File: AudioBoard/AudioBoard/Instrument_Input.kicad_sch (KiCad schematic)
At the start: 3 parts

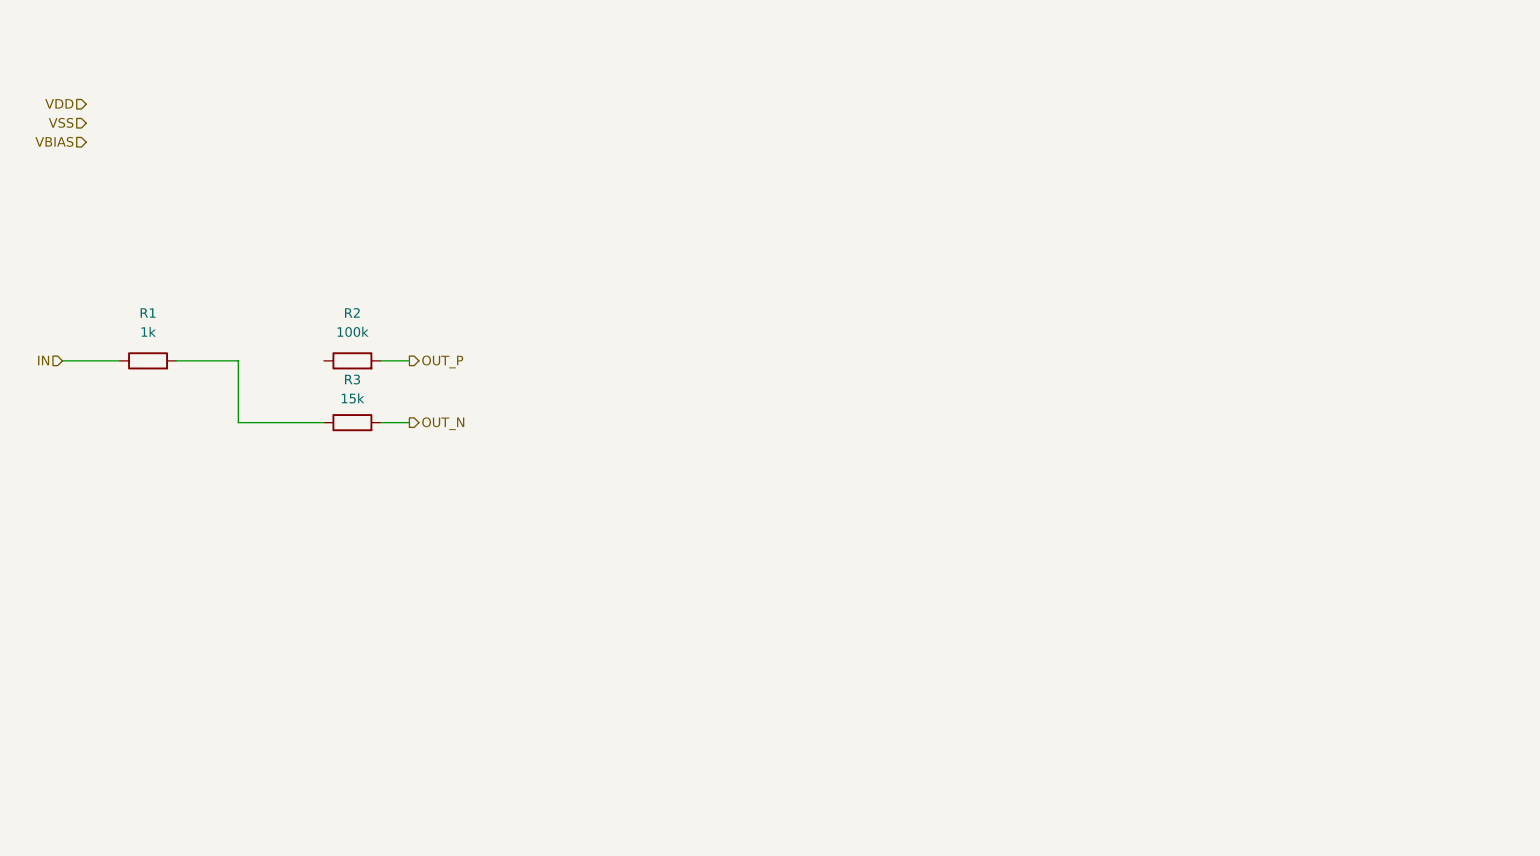
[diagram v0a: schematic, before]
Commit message: added input section
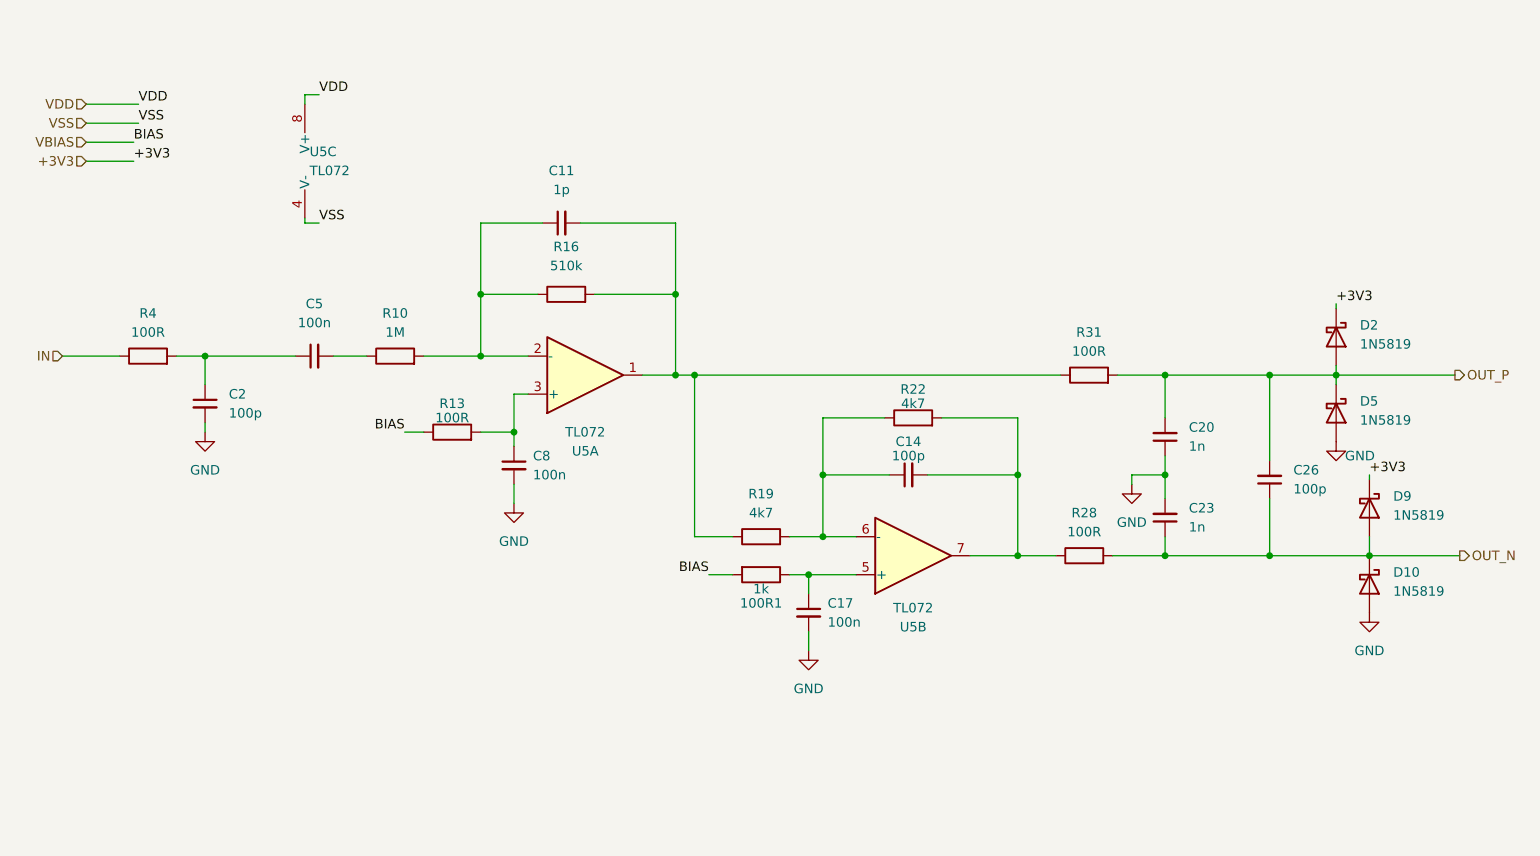
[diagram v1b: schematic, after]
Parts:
- removed R2: 100k, Resistor_SMD:R_0603_1608Metric, symbol Device:R
- removed R3: 15k, Resistor_SMD:R_0603_1608Metric, symbol Device:R
- added 100R1: 1k, Resistor_SMD:R_0603_1608Metric, symbol Device:R
- added C11: 1p, symbol Device:C_Small
- added C14, C2, C26: 100p, symbol Device:C_Small
- added C17, C5, C8: 100n, symbol Device:C_Small
- added C20, C23: 1n, symbol Device:C_Small
- added D10, D2, D5, D9: 1N5819, Diode_THT:D_DO-41_SOD81_P10.16mm_Horizontal, symbol Diode:1N5819
- added R10: 1M, Resistor_SMD:R_0603_1608Metric, symbol Device:R
- added R13, R28, R31: 100R, Resistor_SMD:R_0603_1608Metric, symbol Device:R
- added R16: 510k, Resistor_SMD:R_0603_1608Metric, symbol Device:R
- added R19, R22: 4k7, Resistor_SMD:R_0603_1608Metric, symbol Device:R
- added U5: TL072, Package_SO:SOIC-8_3.9x4.9mm_P1.27mm, symbol Amplifier_Operational:TL072
- R4: renamed from R1; value 1k -> 100R
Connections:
- net OUT_N: now also C23.1, C26.1, D10.1 (K), D9.2 (A), R28.2
- net OUT_P: now also C20.2, C26.2, D2.2 (A), D5.1 (K), R31.2
- net VBIAS: now also 100R1.2, R13.1
- net VDD: now also U5.8 (V+)
- net VSS: now also U5.4 (V-)
- net at R4.2: now also C2.1, C5.1
- new net: C5.2, R10.1
- new net: C11.1, R10.2, R16.1, U5.2 (-)
- new net: C11.2, R16.2, R19.1, R31.1, U5.1
- new net: C8.1, R13.2, U5.3 (+)
- new net: 100R1.1, C17.1, U5.5 (+)
- new net: C14.1, R19.2, R22.1, U5.6 (-)
- new net: C14.2, R22.2, R28.1, U5.7
- new net +3V3: D2.1 (K), D9.1 (K)
- new net GND: C17.2, C2.2, C20.1, C23.2, C8.2, D10.2 (A), D5.2 (A)
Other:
- moved on the sheet: R4

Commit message: input section with templates are working
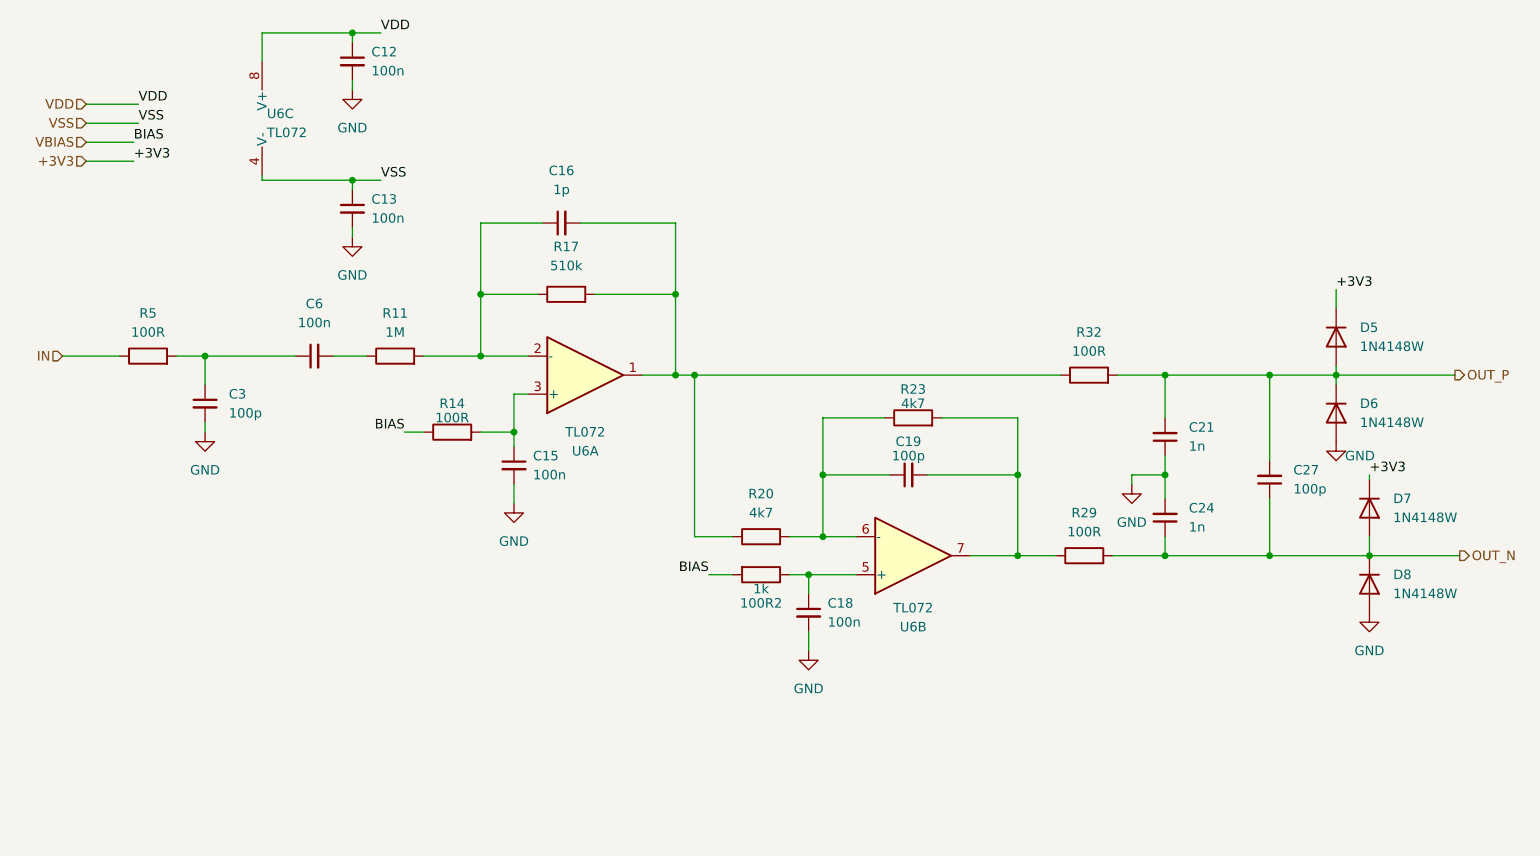
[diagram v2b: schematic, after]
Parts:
- removed D10, D2, D5, D9: 1N5819, Diode_THT:D_DO-41_SOD81_P10.16mm_Horizontal, symbol Diode:1N5819
- added C12, C13: 100n, Capacitor_SMD:C_0402_1005Metric, symbol Device:C_Small
- added D5, D6, D7, D8: 1N4148W, Diode_SMD:D_SOD-123, symbol Diode:1N4148W
- 100R2: renamed from 100R1; footprint Resistor_SMD:R_0603_1608Metric -> Resistor_SMD:R_0402_1005Metric
- C15: renamed from C8; footprint (none) -> Capacitor_SMD:C_0402_1005Metric
- C16: renamed from C11; footprint (none) -> Capacitor_SMD:C_0402_1005Metric
- C18: renamed from C17; footprint (none) -> Capacitor_SMD:C_0402_1005Metric
- C19: renamed from C14; footprint (none) -> Capacitor_SMD:C_0402_1005Metric
- C21: renamed from C20; footprint (none) -> Capacitor_SMD:C_0402_1005Metric
- C24: renamed from C23; footprint (none) -> Capacitor_SMD:C_0402_1005Metric
- C27: renamed from C26; footprint (none) -> Capacitor_SMD:C_0402_1005Metric
- C3: renamed from C2; footprint (none) -> Capacitor_SMD:C_0402_1005Metric
- C6: renamed from C5; footprint (none) -> Capacitor_SMD:C_0402_1005Metric
- R11: renamed from R10; footprint Resistor_SMD:R_0603_1608Metric -> Resistor_SMD:R_0402_1005Metric
- R14: renamed from R13; footprint Resistor_SMD:R_0603_1608Metric -> Resistor_SMD:R_0402_1005Metric
- R17: renamed from R16; footprint Resistor_SMD:R_0603_1608Metric -> Resistor_SMD:R_0402_1005Metric
- R20: renamed from R19; footprint Resistor_SMD:R_0603_1608Metric -> Resistor_SMD:R_0402_1005Metric
- R23: renamed from R22; footprint Resistor_SMD:R_0603_1608Metric -> Resistor_SMD:R_0402_1005Metric
- R29: renamed from R28; footprint Resistor_SMD:R_0603_1608Metric -> Resistor_SMD:R_0402_1005Metric
- R32: renamed from R31; footprint Resistor_SMD:R_0603_1608Metric -> Resistor_SMD:R_0402_1005Metric
- R5: renamed from R4; footprint Resistor_SMD:R_0603_1608Metric -> Resistor_SMD:R_0402_1005Metric
- renumbered U5 to U6
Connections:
- net +3V3: now also D5.1 (K), D7.1 (K)
- net GND: now also C12.2, C13.2, D6.2 (A), D8.2 (A)
- net OUT_N: now also D7.2 (A), D8.1 (K)
- net OUT_P: now also D5.2 (A), D6.1 (K)
- net VDD: now also C12.1
- net VSS: now also C13.1
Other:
- moved on the sheet: U6C

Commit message: Created input sections
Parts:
- 100R2, C12, C13, C15, C16, C18, C19, C21, C24, C27, C3, C6, R11, R14, R17, R20, R23, R29, R32, R5: KiLib_Generator (none) -> SMD_2terminal_chip_molded
- U6: KiLib_Generator (none) -> package/gullwing
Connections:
- net +3V3 renamed AVDD
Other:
- moved on the sheet: C12, C13, U6C

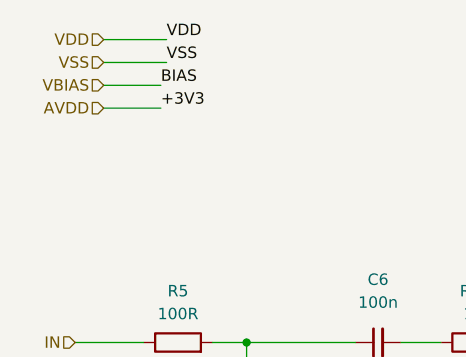
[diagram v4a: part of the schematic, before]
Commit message: added xlr output stage
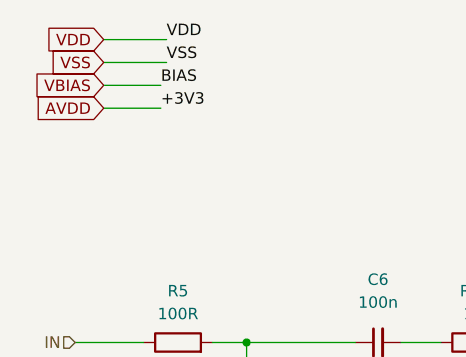
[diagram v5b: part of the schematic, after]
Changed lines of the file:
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@@
 		)
 	)
-	(hierarchical_label "IN"
+	(global_label "VDD"
 		(shape input)
-		(at 34.925 57.785 180)
+		(at 38.1 24.13 180)
+		(fields_autoplaced yes)
 		(effects
 			(font
@@
 			(justify right)
 		)
+		(property "Intersheetrefs" "${INTERSHEET_REFS}"
+			(at 31.4862 24.13 0)
+			(hide yes)
+			(show_name no)
+			(do_not_autoplace no)
+			(effects
+				(font
+					(size 1.27 1.27)
+				)
+				(justify right)
+			)
+		)
 	)
-	(hierarchical_label "VSS"
+	(global_label "AVDD"
 		(shape input)
-		(at 38.1 26.67 180)
+		(at 38.1 31.75 180)
+		(fields_autoplaced yes)
 		(effects
 			(font
@@
 			(justify right)
 		)
+		(property "Intersheetrefs" "${INTERSHEET_REFS}"
+			(at 30.3976 31.75 0)
+			(hide yes)
+			(show_name no)
+			(do_not_autoplace no)
+			(effects
+				(font
+					(size 1.27 1.27)
+				)
+				(justify right)
+			)
+		)
 	)
-	(hierarchical_label "VDD"
+	(global_label "VBIAS"
 		(shape input)
-		(at 38.1 24.13 180)
+		(at 38.1 29.21 180)
+		(fields_autoplaced yes)
+		(effects
+			(font
+				(size 1.27 1.27)
+			)
+			(justify right)
+		)
+		(property "Intersheetrefs" "${INTERSHEET_REFS}"
+			(at 29.8533 29.21 0)
+			(hide yes)
+			(show_name no)
+			(do_not_autoplace no)
+			(effects
+				(font
+					(size 1.27 1.27)
+				)
+				(justify right)
+			)
+		)
+	)
+	(global_label "VSS"
+		(shape input)
+		(at 38.1 26.67 180)
+		(fields_autoplaced yes)
+		(effects
+			(font
+				(size 1.27 1.27)
+			)
+			(justify right)
+		)
+		(property "Intersheetrefs" "${INTERSHEET_REFS}"
+			(at 31.6072 26.67 0)
+			(hide yes)
+			(show_name no)
+			(do_not_autoplace no)
+			(effects
+				(font
+					(size 1.27 1.27)
+				)
+				(justify right)
+			)
+		)
+	)
+	(hierarchical_label "IN"
+		(shape input)
+		(at 34.925 57.785 180)
 		(effects
 			(font
@@
 		)
 	)
-	(hierarchical_label "VBIAS"
-		(shape input)
-		(at 38.1 29.21 180)
-		(effects
-			(font
-				(size 1.27 1.27)
-			)
-			(justify right)
-		)
-	)
 	(hierarchical_label "OUT_N"
 		(shape output)
@@
 		)
 	)
-	(hierarchical_label "AVDD"
-		(shape input)
-		(at 38.1 31.75 180)
-		(effects
-			(font
-				(size 1.27 1.27)
-			)
-			(justify right)
-		)
-	)

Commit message: added lcscpart to components and assigned footprints
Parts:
- 100R2: JLCPCB (none) -> C11702; LCSC Part (none) -> C11702
- C12, C13, C15, C18, C6: JLCPCB (none) -> C1591; LCSC Part (none) -> C1591
- C16: JLCPCB (none) -> C1550; LCSC Part (none) -> C1550
- C19, C27, C3: JLCPCB (none) -> C1546; LCSC Part (none) -> C1546
- C21, C24: JLCPCB (none) -> C1523; LCSC Part (none) -> C1523
- D5, D6, D7, D8: JLCPCB (none) -> C81598; LCSC Part (none) -> C81598
- R11: JLCPCB (none) -> C26083; LCSC Part (none) -> C26083
- R14, R29, R32, R5: JLCPCB (none) -> C25076; LCSC Part (none) -> C25076
- R17: footprint Resistor_SMD:R_0402_1005Metric -> Resistor_SMD:R_0603_1608Metric; JLCPCB (none) -> C23192; LCSC Part (none) -> C23192
- R20, R23: JLCPCB (none) -> C25900; LCSC Part (none) -> C25900
- U6: JLCPCB (none) -> C6961; LCSC Part (none) -> C6961
